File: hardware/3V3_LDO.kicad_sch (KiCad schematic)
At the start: 5 parts, among them U5 MCP1826S

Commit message: schem except BQ
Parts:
- renumbered C27 to C31, C28 to C32, D11 to D3
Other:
- moved on the sheet: C31, C32, D3, TP_3.3V1, U5

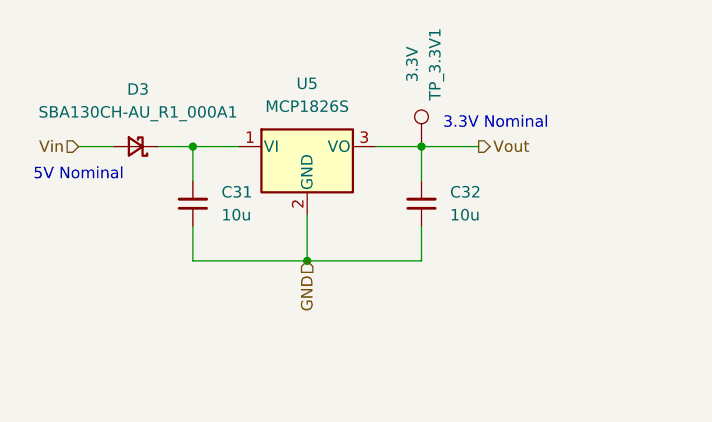
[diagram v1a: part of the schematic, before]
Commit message: New BMS arch and IC
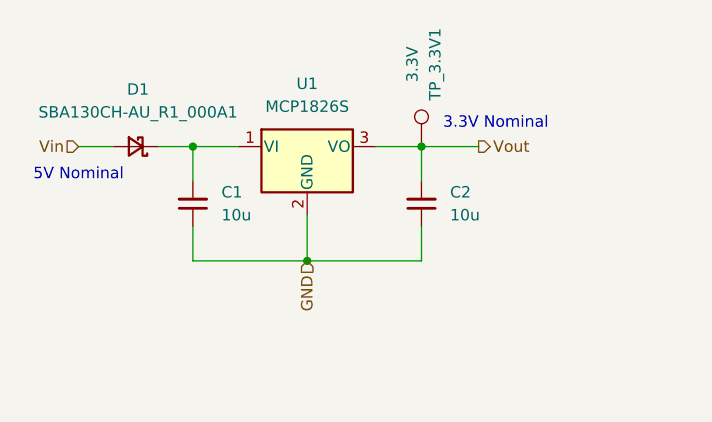
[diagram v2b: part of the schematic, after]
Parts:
- renumbered C31 to C1, C32 to C2, D3 to D1, U5 to U1
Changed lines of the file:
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@@
 		(dnp no)
 		(fields_autoplaced yes)
-		(property "Reference" "C32"
+		(property "Reference" "C2"
 			(at 113.665 80.0035 0)
 			(show_name no)
@@
 		)
 		(instances
-			(project "LDO"
-				(path "/8ff43370-8d10-4d2c-b1a3-81d1c2934a98"
+			(project "PS-SegmentMonitoringBoard"
+				(path "/f5c3f134-fd91-4d3b-aae6-719b554b2d69/c374ccb1-3fca-459f-ad5f-933aa5d7a29c/a818c6fb-3bbd-452d-9e3e-0949d081e2ed"
 					(reference "C2")
-					(unit 1)
-				)
-			)
-			(project "LeaderSOMBreakout"
-				(path "/e5b32072-3e3d-42a6-9d41-1a76d538e329/f3053c74-1ac6-4a33-80f3-565e8c4c2c7d"
-					(reference "C?")
-					(unit 1)
-				)
-			)
-			(project "PS-SegmentMonitoringBoard"
-				(path "/f5c3f134-fd91-4d3b-aae6-719b554b2d69/0f853b25-e2f5-4198-b067-37aee21ed095"
-					(reference "C32")
 					(unit 1)
 				)
@@
 		)
 		(instances
-			(project "LDO"
-				(path "/8ff43370-8d10-4d2c-b1a3-81d1c2934a98"
-					(reference "TP_3.3V1")
-					(unit 1)
-				)
-			)
 			(project "PS-SegmentMonitoringBoard"
-				(path "/f5c3f134-fd91-4d3b-aae6-719b554b2d69/0f853b25-e2f5-4198-b067-37aee21ed095"
+				(path "/f5c3f134-fd91-4d3b-aae6-719b554b2d69/c374ccb1-3fca-459f-ad5f-933aa5d7a29c/a818c6fb-3bbd-452d-9e3e-0949d081e2ed"
 					(reference "TP_3.3V1")
 					(unit 1)
@@
 		(dnp no)
 		(fields_autoplaced yes)
-		(property "Reference" "U5"
+		(property "Reference" "U1"
 			(at 97.79 67.945 0)
 			(show_name no)
@@
 		)
 		(instances
-			(project ""
-				(path "/8ff43370-8d10-4d2c-b1a3-81d1c2934a98"
+			(project "PS-SegmentMonitoringBoard"
+				(path "/f5c3f134-fd91-4d3b-aae6-719b554b2d69/c374ccb1-3fca-459f-ad5f-933aa5d7a29c/a818c6fb-3bbd-452d-9e3e-0949d081e2ed"
 					(reference "U1")
-					(unit 1)
-				)
-			)
-			(project "PS-SegmentMonitoringBoard"
-				(path "/f5c3f134-fd91-4d3b-aae6-719b554b2d69/0f853b25-e2f5-4198-b067-37aee21ed095"
-					(reference "U5")
 					(unit 1)
 				)
@@
 		(dnp no)
 		(fields_autoplaced yes)
-		(property "Reference" "D3"
+		(property "Reference" "D1"
 			(at 78.994 68.58 0)
 			(show_name no)
@@
 		)
 		(instances
-			(project ""
-				(path "/8ff43370-8d10-4d2c-b1a3-81d1c2934a98"
+			(project "PS-SegmentMonitoringBoard"
+				(path "/f5c3f134-fd91-4d3b-aae6-719b554b2d69/c374ccb1-3fca-459f-ad5f-933aa5d7a29c/a818c6fb-3bbd-452d-9e3e-0949d081e2ed"
 					(reference "D1")
-					(unit 1)
-				)
-			)
-			(project "PS-SegmentMonitoringBoard"
-				(path "/f5c3f134-fd91-4d3b-aae6-719b554b2d69/0f853b25-e2f5-4198-b067-37aee21ed095"
-					(reference "D3")
 					(unit 1)
 				)
@@
 		(dnp no)
 		(fields_autoplaced yes)
-		(property "Reference" "C31"
+		(property "Reference" "C1"
 			(at 88.265 80.0035 0)
 			(show_name no)
@@
 		)
 		(instances
-			(project "LDO"
-				(path "/8ff43370-8d10-4d2c-b1a3-81d1c2934a98"
+			(project "PS-SegmentMonitoringBoard"
+				(path "/f5c3f134-fd91-4d3b-aae6-719b554b2d69/c374ccb1-3fca-459f-ad5f-933aa5d7a29c/a818c6fb-3bbd-452d-9e3e-0949d081e2ed"
 					(reference "C1")
 					(unit 1)
 				)
-			)
-			(project ""
-				(path "/e5b32072-3e3d-42a6-9d41-1a76d538e329/f3053c74-1ac6-4a33-80f3-565e8c4c2c7d"
-					(reference "C?")
-					(unit 1)
-				)
-			)
-			(project "PS-SegmentMonitoringBoard"
-				(path "/f5c3f134-fd91-4d3b-aae6-719b554b2d69/0f853b25-e2f5-4198-b067-37aee21ed095"
-					(reference "C31")
-					(unit 1)
-				)
